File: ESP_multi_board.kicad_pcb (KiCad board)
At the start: 2 copper layers, 24 parts, among them P101 CONN_01X02, P102 CONN_01X06, P103 CONN_01X02, P104 CONN_01X06, P105 CONN_01X12, P106 CONN_01X03, P107 CONN_I2C_MPU6050, P108 CONN_PINES_DIG, SW101 SW_PUSH_SMALL, SW102 SWITCH_INV, U1 LD1117S33TR, U101 L293DD, U102 ESP-12, U103 MAX11605EEE+, U104 MCP23008

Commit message: routing
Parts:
- added D101: D, Diodes_ThroughHole:Diode_DO-35_SOD27_Horizontal_RM10, F.Cu at (162.4, 86.6)
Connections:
- P101 pad 2: Net-(P101-Pad2) -> Net-(D101-Pad1)
- SW102 pad 2: Net-(P101-Pad2) -> Net-(D101-Pad2)

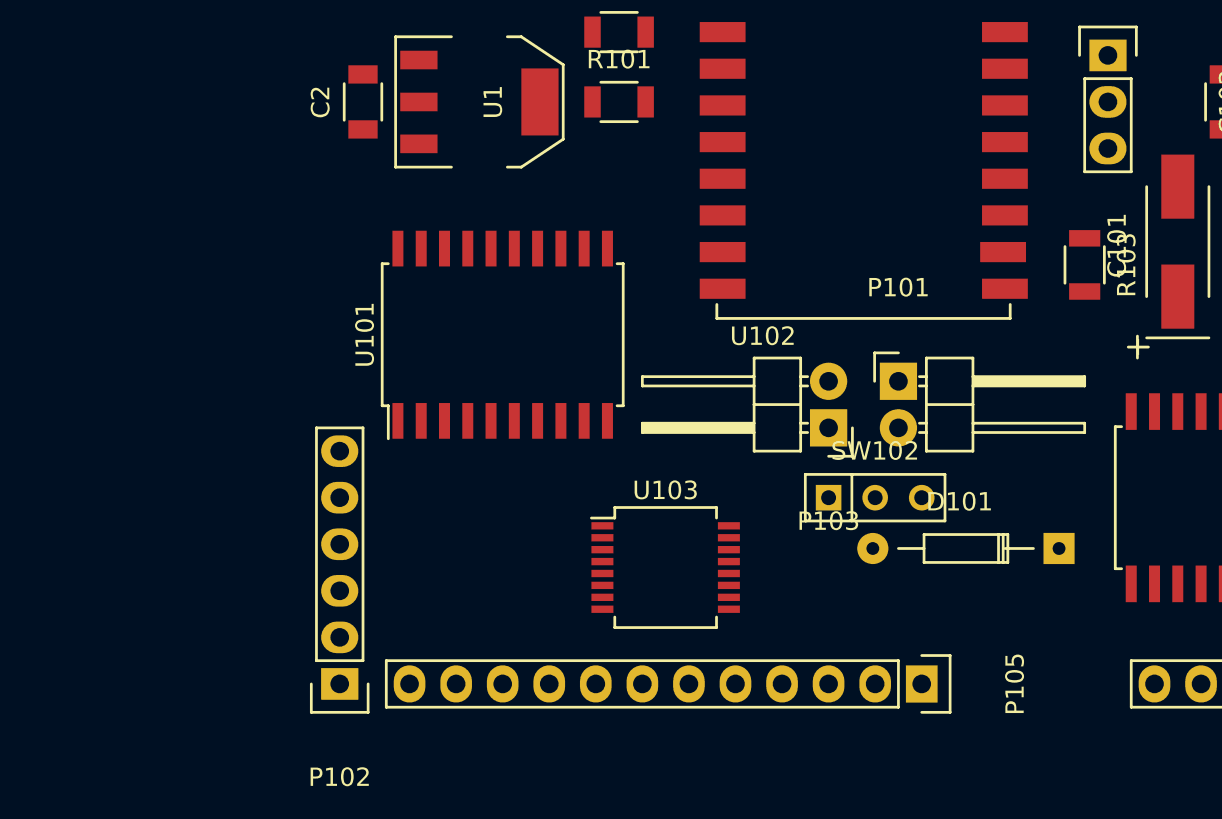
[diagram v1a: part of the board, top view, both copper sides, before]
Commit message: huellas diodos actualizadas
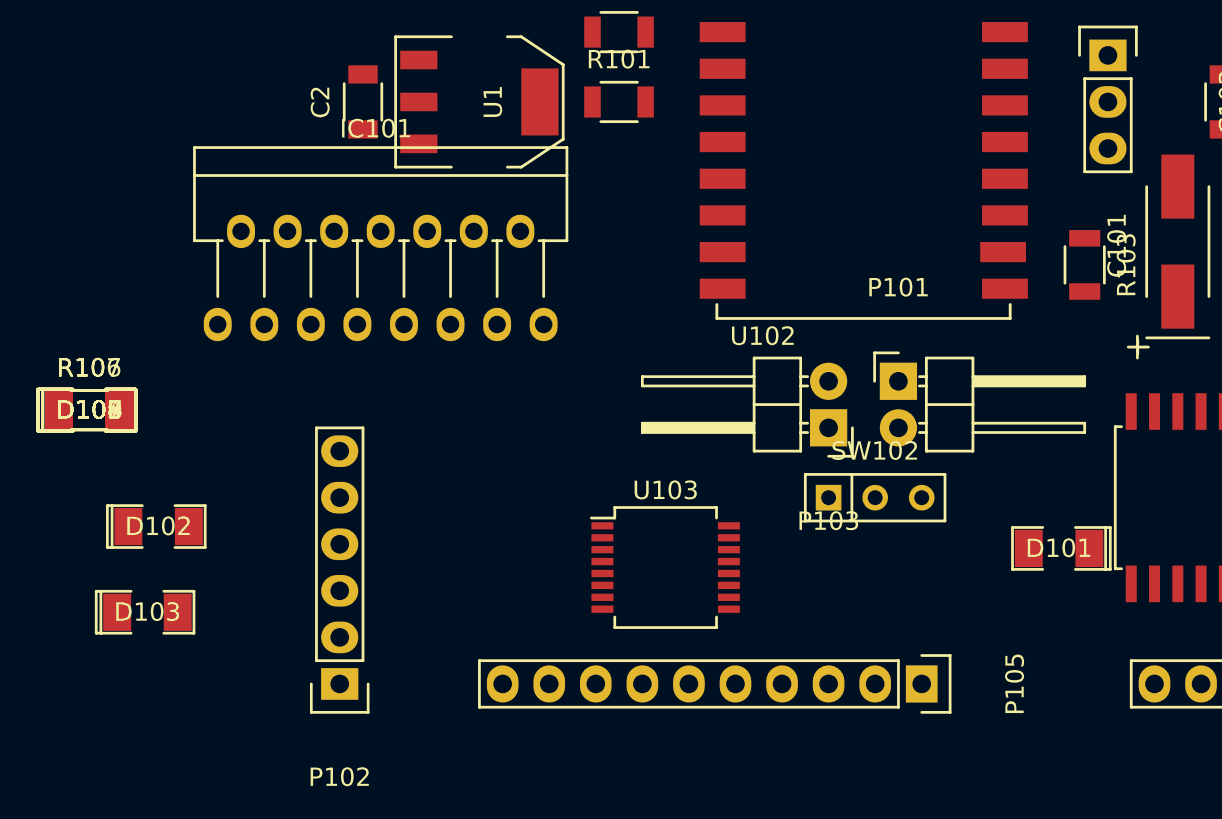
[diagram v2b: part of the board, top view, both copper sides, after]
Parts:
- removed U101: L293DD, Housings_SOIC:SOIC-20_7.5x12.8mm_Pitch1.27mm
- added D102: D, SMD_Packages:SMD-1206_Pol, F.Cu at (113.3, 85.4)
- added D103: D, SMD_Packages:SMD-1206_Pol, F.Cu at (112.7, 90.1)
- added D104, D105, D106, D107, D108, D109: D, SMD_Packages:SMD-1206_Pol, F.Cu at (109.5, 79.0)
- added IC101: L298, TO_SOT_Packages_THT:Multiwatt_15_Vertical, F.Cu at (116.5, 74.4)
- added R106, R107: 0.5, Resistors_SMD:R_1206, F.Cu at (109.5, 79.0)
- D101: footprint Diodes_ThroughHole:Diode_DO-35_SOD27_Horizontal_RM10 -> SMD_Packages:SMD-1206_Pol
- P105: footprint Pin_Headers:Pin_Header_Straight_1x12 -> Pin_Headers:Pin_Header_Straight_1x10
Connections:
- U103 pad 1: Net-(P105-Pad12) -> CURRENT1
- U103 pad 2: Net-(P105-Pad11) -> CURRENT2

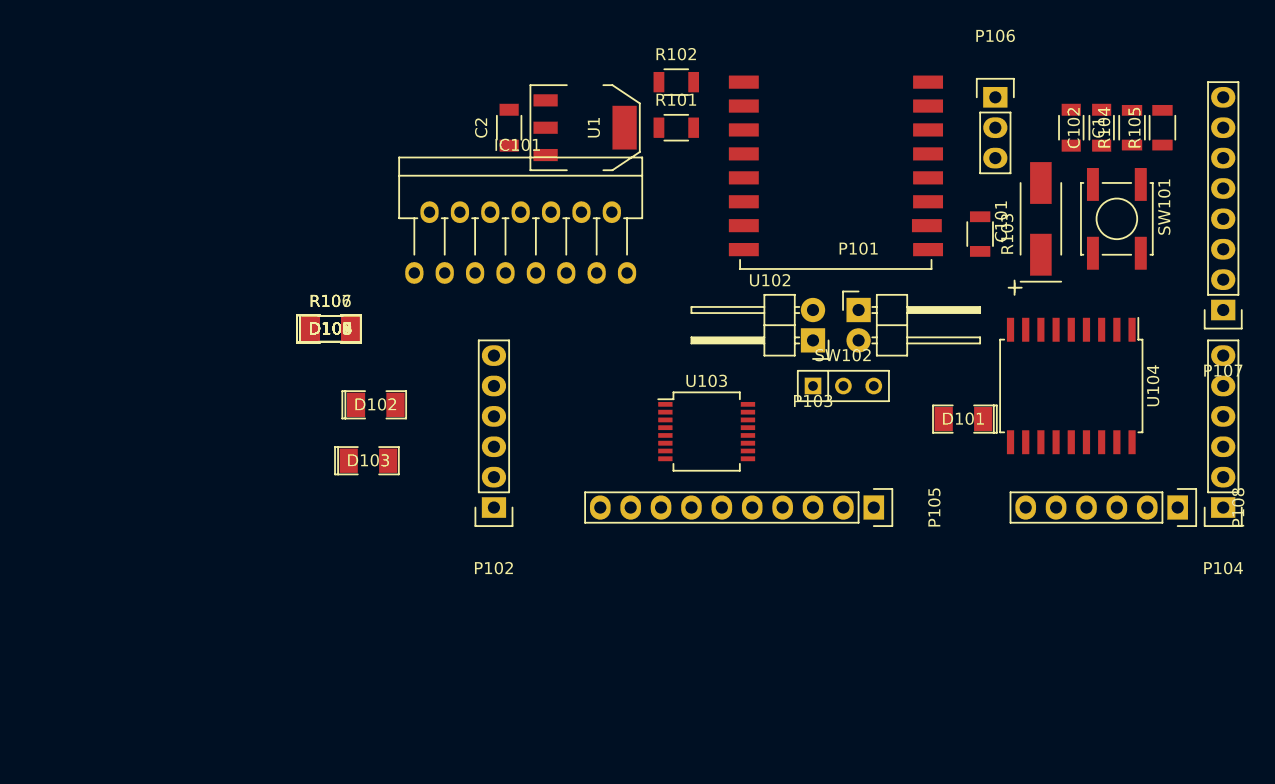
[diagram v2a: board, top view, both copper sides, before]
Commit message: nueva placa con hueco para motores integrado
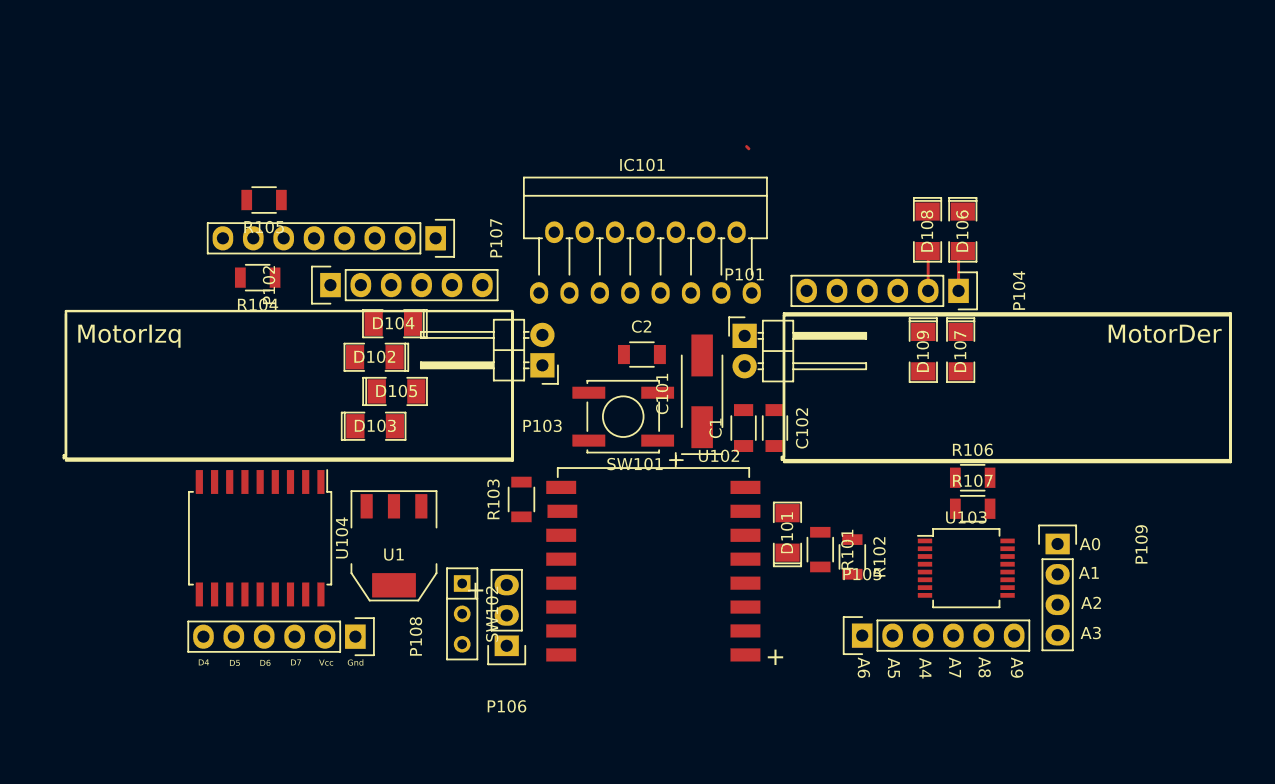
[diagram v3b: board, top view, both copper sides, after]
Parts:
- added P109: CONN_01X04, Socket_Strips:Socket_Strip_Straight_1x04, F.Cu at (170.3, 97.0)
- P105: value CONN_01X12 -> CONN_01X06; footprint Pin_Headers:Pin_Header_Straight_1x10 -> Socket_Strips:Socket_Strip_Straight_1x06
- moved R105 75.3 mm to (104.0, 68.3), turned to 180 degrees
- moved R104 74.2 mm to (103.4, 74.8), turned to 180 degrees
- moved P108 69.6 mm to (111.6, 104.8)
- moved U104 69.0 mm to (103.6, 96.5)
- moved P107 66.1 mm to (118.3, 71.5), turned to 270 degrees
- moved P106 61.4 mm to (124.3, 105.5), turned to 180 degrees
- moved R107 55.7 mm to (163.2, 94.1)
- moved R106 55.1 mm to (163.2, 91.5)
- moved D106 53.5 mm to (162.4, 70.9), turned to 270 degrees
- moved D107 52.7 mm to (162.2, 80.9), turned to 270 degrees
- moved D108 50.6 mm to (159.4, 70.9), turned to 270 degrees
- moved D109 49.6 mm to (159.1, 80.9), turned to 270 degrees
- moved U102 47.9 mm to (143.5, 106.3), turned to 180 degrees
- moved SW101 44.5 mm to (134.0, 86.4), turned to 180 degrees
- moved R103 44.3 mm to (125.5, 93.3), turned to 90 degrees
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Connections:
- P102 pad 3: VDD -> ENC1_A
- P102 pad 4: GND -> ENC1_B
- P102 pad 5: ENC1_A -> VDD
- P102 pad 6: ENC1_B -> GND
- P104 pad 3: VDD -> ENC2_A
- P104 pad 4: GND -> ENC2_B
- P104 pad 5: ENC2_A -> VDD
- P104 pad 6: ENC2_B -> GND
- U103 pad 10: Net-(P105-Pad3) -> Net-(P109-Pad3)
- U103 pad 11: Net-(P105-Pad2) -> Net-(P109-Pad2)
- U103 pad 12: Net-(P105-Pad1) -> Net-(P109-Pad1)
- U103 pad 3: Net-(P105-Pad10) -> Net-(P105-Pad6)
- U103 pad 4: Net-(P105-Pad9) -> Net-(P105-Pad5)
- U103 pad 5: Net-(P105-Pad8) -> Net-(P105-Pad4)
- U103 pad 6: Net-(P105-Pad5) -> Net-(P105-Pad1)
- U103 pad 7: Net-(P105-Pad6) -> Net-(P105-Pad2)
- U103 pad 8: Net-(P105-Pad7) -> Net-(P105-Pad3)
- U103 pad 9: Net-(P105-Pad4) -> Net-(P109-Pad4)
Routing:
- net M2+: track 0.00 -> 3.47 mm
- net M2-: track 0.00 -> 3.35 mm
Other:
- net class Default: clearance 0.3 -> 0.25; trace_width 0.3 -> 0.25
- net class power: trace_width 0.5 -> 0.25
- rule trace_clearance: 0.3 -> 0.25
- rule trace_min: 0.3 -> 0.25
- board text added: "+"
- board text added: "A0"
- board text added: "A1"
- board text added: "A2"
- board text added: "A3"
- board text added: "A4"
- board text added: "A5"
- board text added: "A6"
- board text added: "A7"
- board text added: "A8"
- board text added: "A9"
- board text added: "D4"
- board text added: "D5"
- board text added: "D6"
- board text added: "D7"
- board text added: "Gnd"
- board text added: "MotorDer"
- board text added: "MotorIzq"
- board text added: "Vcc"

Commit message: motores mas juntos en la PCB
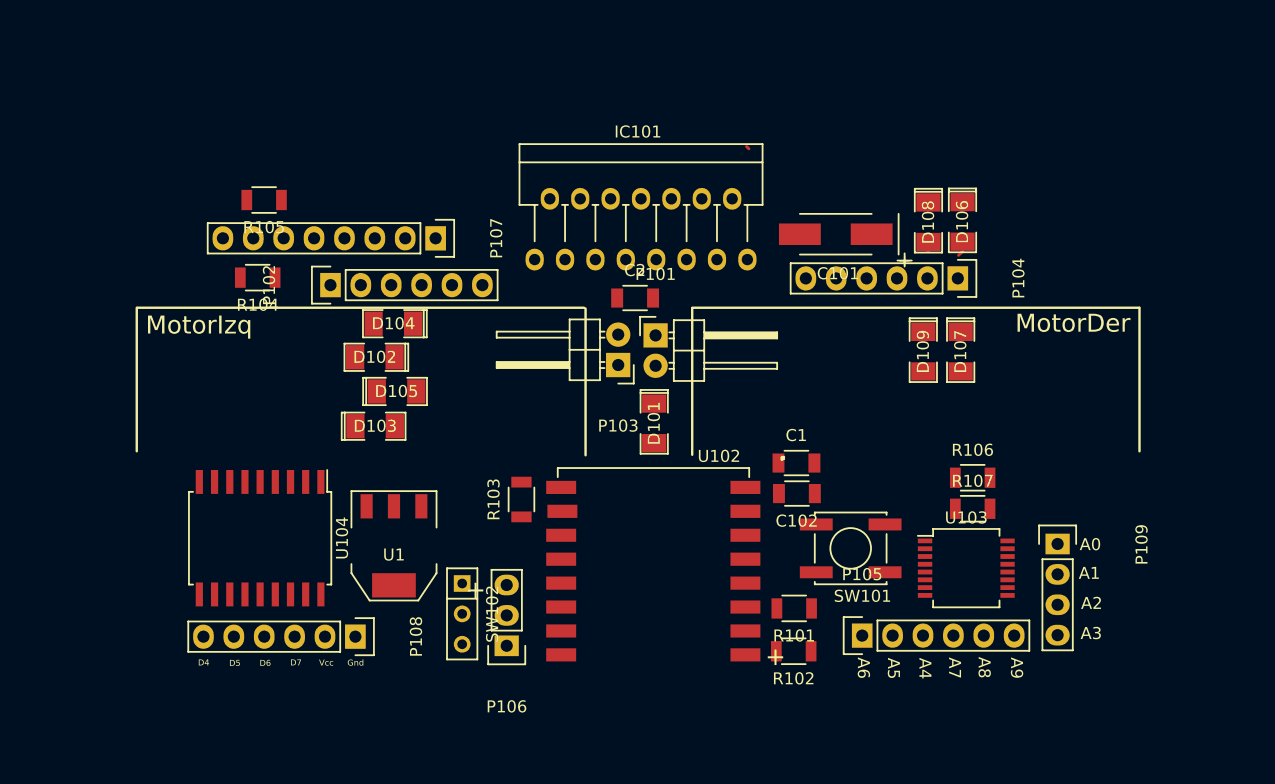
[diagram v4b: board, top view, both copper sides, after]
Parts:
- moved SW101 22.0 mm to (153.0, 97.4)
- moved C101 17.2 mm to (151.8, 71.1), turned to 180 degrees
- moved D101 14.4 mm to (136.6, 86.9), turned to 270 degrees
- moved R102 9.29 mm to (148.2, 106.0), turned to 180 degrees
- moved P101 7.44 mm to (136.7, 79.6)
- moved P103 6.34 mm to (133.6, 82.1)
- moved C102 5.77 mm to (148.5, 92.8), turned to 180 degrees
- moved R101 5.38 mm to (148.3, 102.4), turned to 180 degrees
- moved C1 5.30 mm to (148.5, 90.3), turned to 0 degrees
- moved C2 4.76 mm to (135.0, 76.5)
- moved IC101 2.82 mm to (126.6, 73.3)
- moved P104 1.04 mm to (162.0, 74.8)
- moved D106 0.79 mm to (162.4, 70.1)
- moved D108 0.77 mm to (159.5, 70.1)
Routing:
- net M2+: track 3.47 -> 0.00 mm
- net M2-: track 3.35 -> 0.07 mm
- net (no net): track 0.27 -> 0.77 mm

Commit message: Actualizadas huellas de acuerdo a los componentes de Mouser
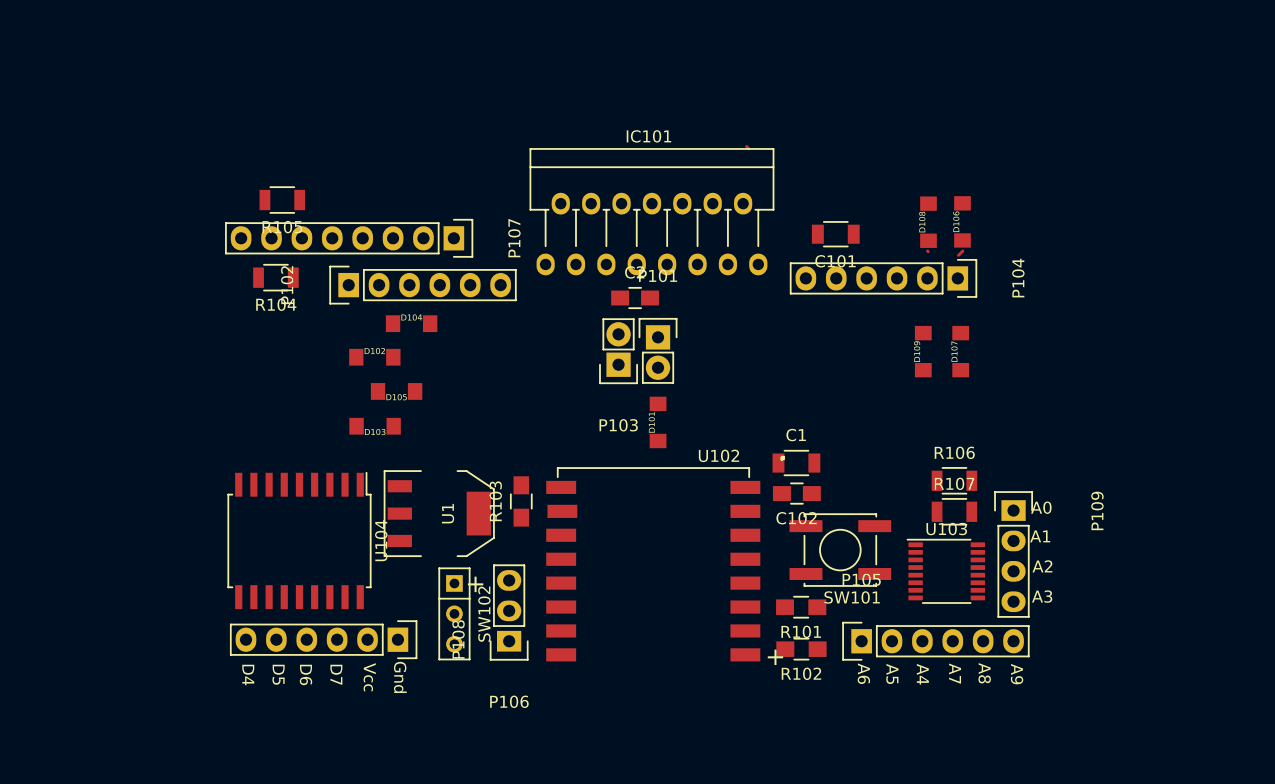
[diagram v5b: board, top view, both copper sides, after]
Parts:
- C101: footprint Capacitors_Tantalum_SMD:TantalC_SizeC_EIA-6032_HandSoldering -> Capacitors_SMD:C_1206
- C102, C2: footprint Capacitors_SMD:C_1206 -> Capacitors_SMD:C_0805_HandSoldering
- D101, D102, D103, D104, D105, D106, D107, D108, D109: footprint SMD_Packages:SMD-1206_Pol -> diodos_smd:SMD_D_SMA-Sub-2
- P101, P103: footprint Pin_Headers:Pin_Header_Angled_1x02 -> Pin_Headers:Pin_Header_Straight_1x02
- R101, R102, R103: footprint Resistors_SMD:R_1206 -> Resistors_SMD:R_0805_HandSoldering
- U103: footprint Housings_SSOP:SSOP-16_5.3x6.2mm_Pitch0.65mm -> Housings_SSOP:SSOP-16_3.9x4.9mm_Pitch0.635mm
- moved U1 4.64 mm to (118.6, 94.5), turned to 270 degrees
- moved P109 4.62 mm to (166.6, 94.2)
- moved P108 3.57 mm to (115.2, 105.0)
- moved U104 3.30 mm to (106.9, 96.8)
- moved U103 1.66 mm to (161.0, 99.3)
- moved R106 1.55 mm to (161.7, 91.7)
- moved R107 1.55 mm to (161.7, 94.3)
- moved D104 1.52 mm to (116.3, 78.6)
- moved P102 1.52 mm to (111.0, 75.4)
- moved P107 1.52 mm to (119.8, 71.5)
- moved R104 1.52 mm to (105.0, 74.8)
- moved R105 1.52 mm to (105.5, 68.3)
- moved IC101 1.00 mm to (127.5, 73.7)
- moved SW101 0.87 mm to (152.1, 97.5)
- moved R102 0.67 mm to (148.9, 105.8)
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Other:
- board text added: "MPU6050"

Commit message: placa actualizada
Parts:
- removed D101: D, diodos_smd:SMD_D_SMA-Sub-2
- added REF**: troquel, taladros:troquel_3, F.Cu at (99.5, 69.5)
- added REF** (x2): troquel, taladros:troquel_3, F.Cu at (172.2, 87.2)
- added REF** (x2): troquel, taladros:troquel_3, F.Cu at (172.2, 78.5)
- added REF** (x2): troquel, taladros:troquel_3, F.Cu at (172.2, 69.8)
- added REF** (x2): troquel, taladros:troquel_3, F.Cu at (172.2, 110.5)
- added REF** (x2): troquel, taladros:troquel_3, F.Cu at (172.2, 104.5)
- added REF**: 1pin, Connect:1pin, F.Cu at (175.0, 93.0)
- added REF**: 1pin, Connect:1pin, F.Cu at (175.0, 77.2)
- added REF**: troquel, taladros:troquel_3, F.Cu at (99.5, 75.5)
- added REF**: 1pin, Connect:1pin, F.Cu at (149.3, 110.0)
- added REF**: 1pin, Connect:1pin, F.Cu at (124.0, 110.0)
- added REF** (x2): troquel, taladros:troquel_3, F.Cu at (172.2, 96.0)
- added REF**: troquel, taladros:troquel_3, F.Cu at (99.5, 84.2)
- added REF**: troquel, taladros:troquel_3, F.Cu at (99.5, 93.0)
- added REF**: troquel, taladros:troquel_3, F.Cu at (99.5, 101.8)
- added REF**: troquel, taladros:troquel_3, F.Cu at (99.5, 110.5)
- P101, P103: footprint Pin_Headers:Pin_Header_Straight_1x02 -> Pin_Headers:Pin_Header_Angled_1x02
- P105: footprint Socket_Strips:Socket_Strip_Straight_1x06 -> Pin_Headers:Pin_Header_Straight_1x06
- P107: footprint Pin_Headers:Pin_Header_Straight_1x08 -> Socket_Strips:Socket_Strip_Straight_1x08
- P109: footprint Socket_Strips:Socket_Strip_Straight_1x04 -> Pin_Headers:Pin_Header_Straight_1x04
- R104, R105: value 47k -> 4.7k; footprint Resistors_SMD:R_1206 -> Resistors_SMD:R_0805_HandSoldering
- moved R106 40.6 mm to (125.4, 73.6), turned to 90 degrees
- moved C2 32.9 mm to (115.3, 102.9), turned to 270 degrees
- moved R107 23.2 mm to (147.5, 76.0)
- moved P107 17.7 mm to (102.2, 70.4), turned to 0 degrees
- moved D107 17.7 mm to (149.1, 69.1), turned to 0 degrees
- moved D103 14.7 mm to (109.7, 72.9)
- moved D109 13.8 mm to (149.1, 71.4), turned to 0 degrees
- moved D105 13.4 mm to (105.2, 75.2), turned to 180 degrees
- moved D102 8.98 mm to (105.2, 77.4), turned to 0 degrees
- moved C1 8.11 mm to (155.2, 94.8), turned to 180 degrees
- moved D104 5.80 mm to (115.3, 72.9)
- moved P103 5.73 mm to (132.3, 76.5), turned to 270 degrees
- moved P101 5.04 mm to (140.7, 76.5), turned to 270 degrees
- moved C101 2.77 mm to (154.5, 71.6)
- moved P104 2.63 mm to (164.6, 74.9)
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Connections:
- P101 pad 2: Net-(D101-Pad1) -> Net-(P101-Pad2)
- SW102 pad 2: Net-(D101-Pad2) -> Net-(P101-Pad2)
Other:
- board outline added: 100 x 50 mm
